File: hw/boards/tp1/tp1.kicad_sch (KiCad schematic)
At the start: 17 parts

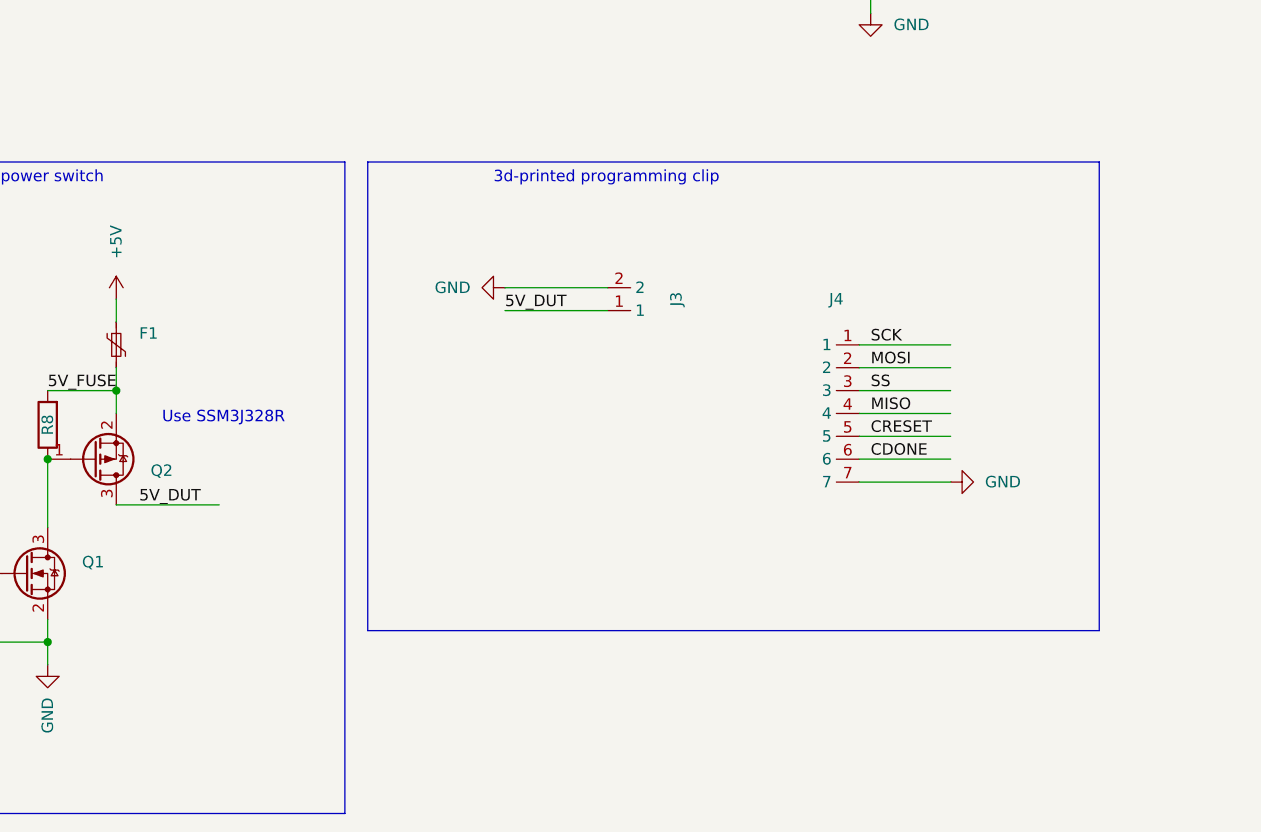
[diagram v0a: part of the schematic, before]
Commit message: TP-1 release: Add screws, feet to the BOM
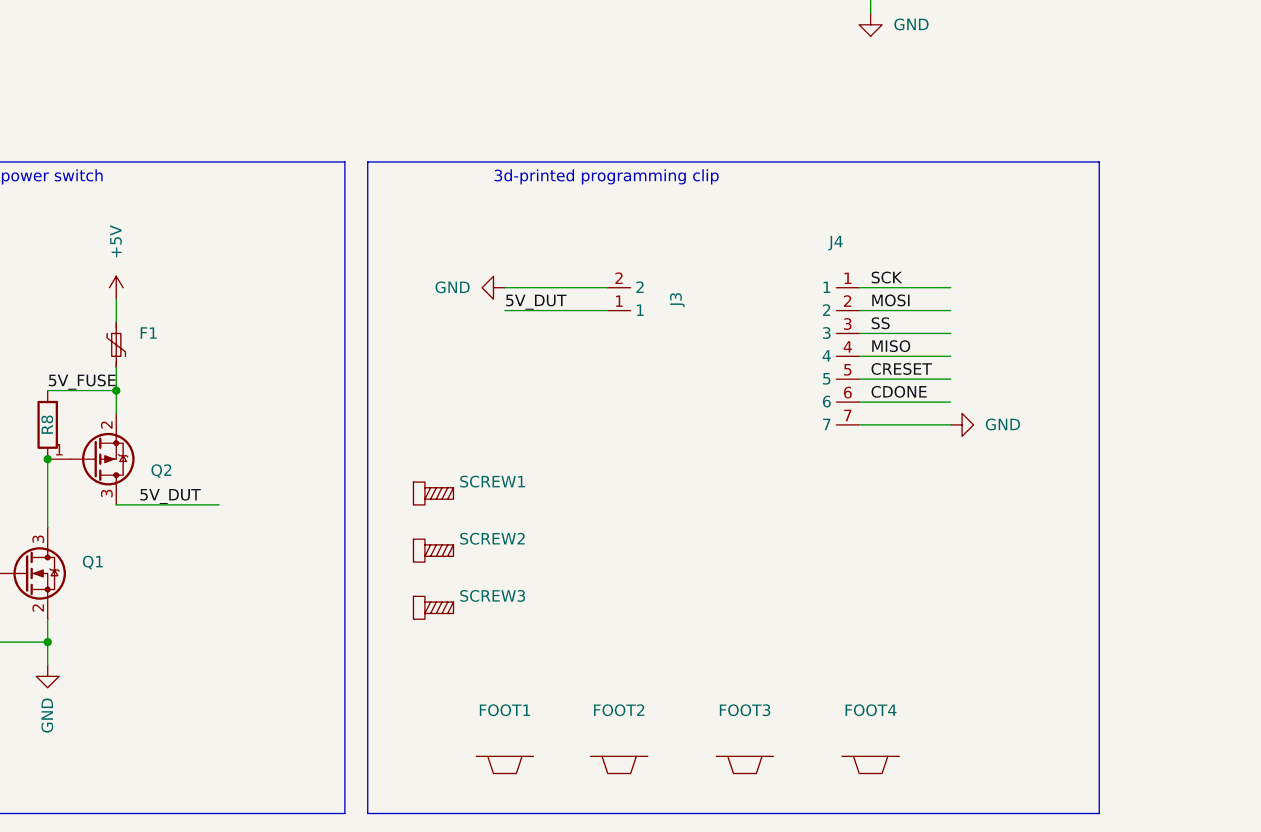
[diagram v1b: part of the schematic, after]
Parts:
- added FOOT1, FOOT2, FOOT3, FOOT4: (no value), symbol mta1:Foot
- added SCREW1, SCREW2, SCREW3: (no value), symbol mta1:Screw
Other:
- note removed: "Use SSM3J328R"
- moved on the sheet: J4

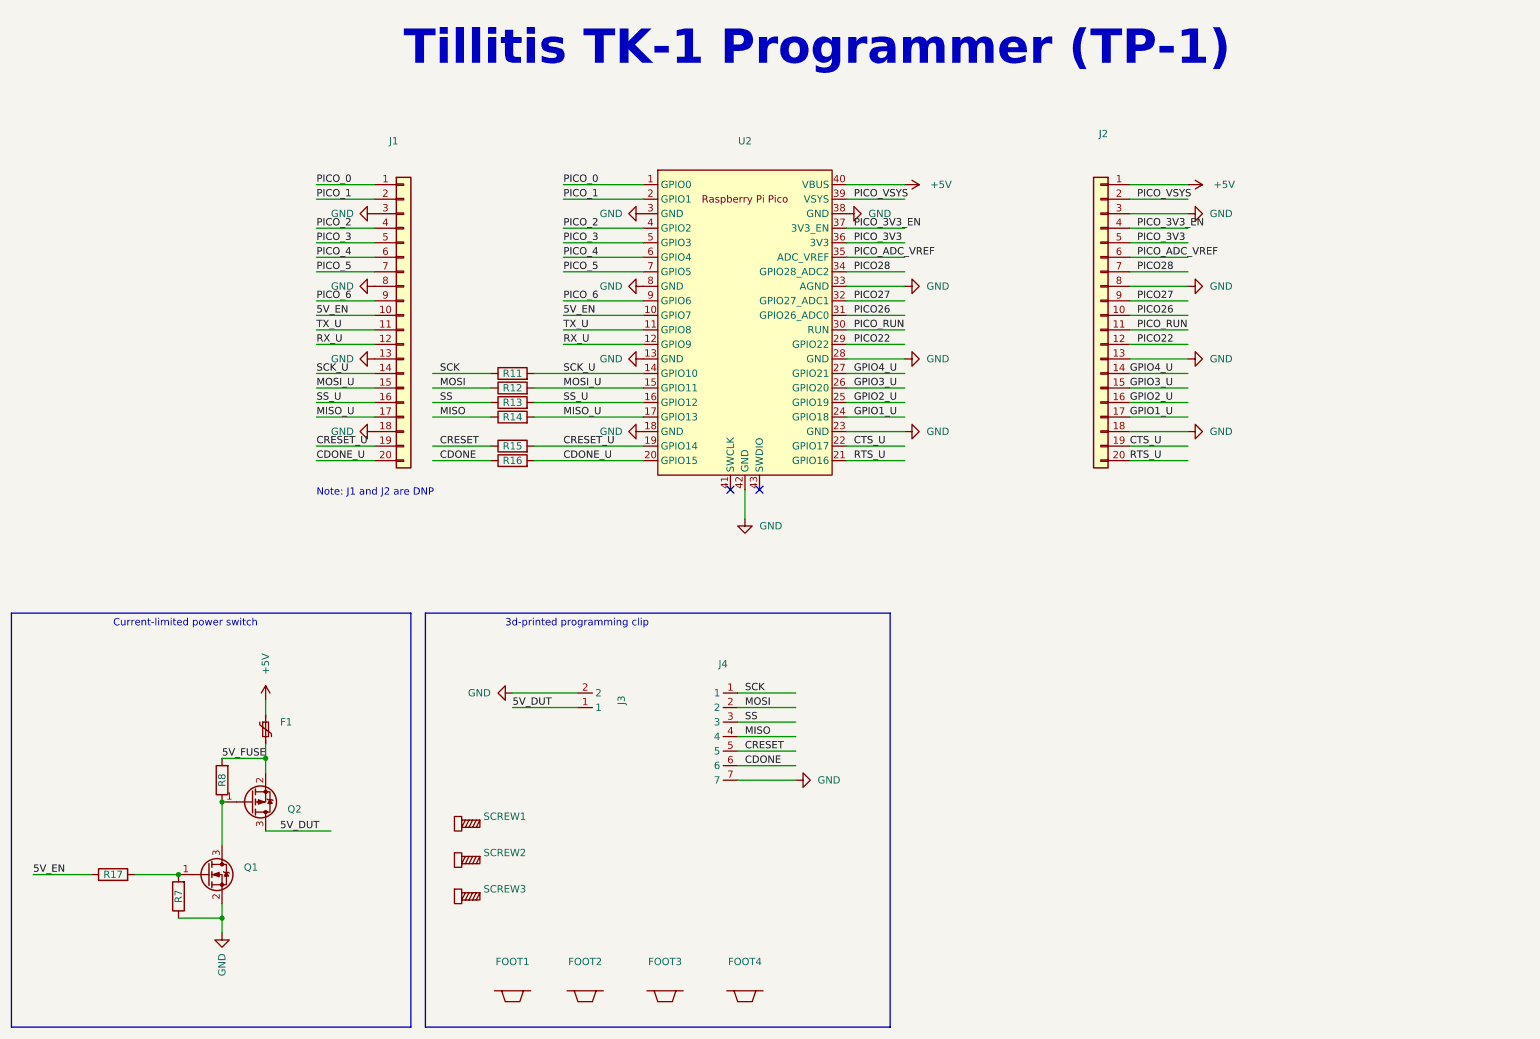
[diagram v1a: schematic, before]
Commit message: TP-1 RevA release updates:
* Add fiducials in 3 corners (1mm exposed copper ring w/2mm soldermask opening)
* Add solder paste openings to Raspberry Pi Pico pads
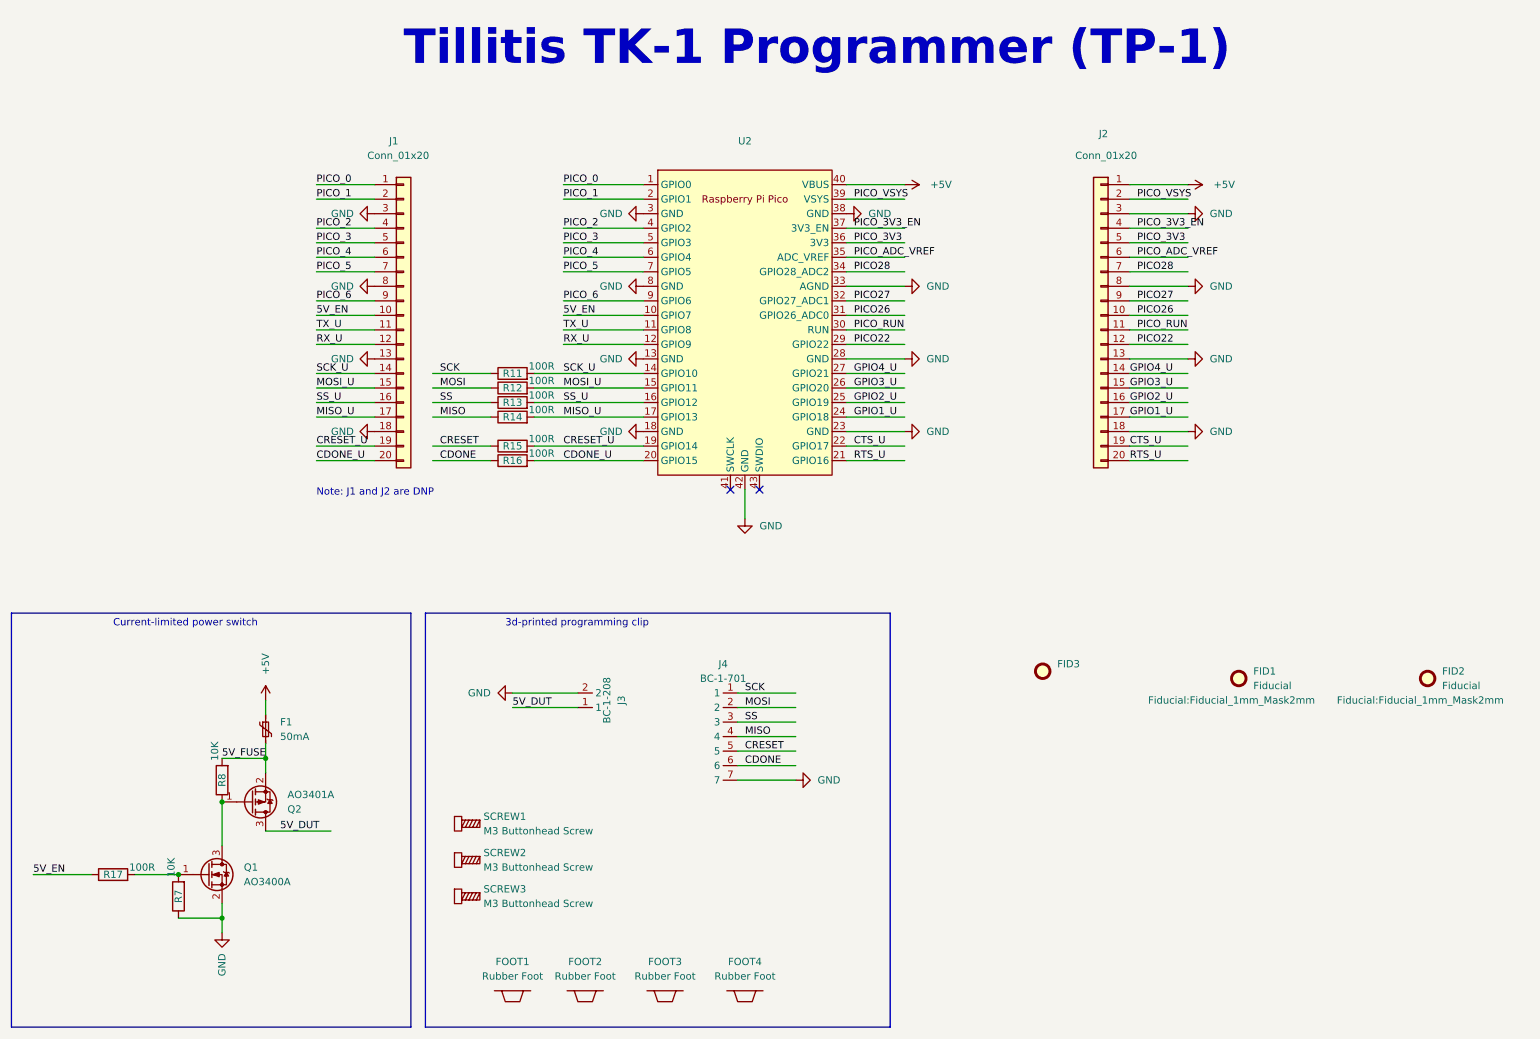
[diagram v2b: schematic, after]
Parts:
- added FID1, FID2: Fiducial, Fiducial:Fiducial_1mm_Mask2mm, symbol Mechanical:Fiducial
- added FID3: (no value), symbol Mechanical:Fiducial
- F1: value (none) -> 50mA; footprint (none) -> Fuse:Fuse_1206_3216Metric
- FOOT1, FOOT2, FOOT3, FOOT4: value (none) -> Rubber Foot
- J1, J2: value (none) -> Conn_01x20; footprint (none) -> Connector_PinHeader_2.54mm:PinHeader_1x20_P2.54mm_Vertical
- J3: value (none) -> BC-1-208; footprint (none) -> mta1:BC-1-208
- J4: value (none) -> BC-1-701; footprint (none) -> mta1:BC-1-701
- Q1: value (none) -> AO3400A; footprint (none) -> Package_TO_SOT_SMD:SOT-23
- Q2: value (none) -> AO3401A; footprint (none) -> Package_TO_SOT_SMD:SOT-23
- R11, R12, R13, R14, R15, R16, R17: value (none) -> 100R; footprint (none) -> mta1:ERJ2G(0402)_L
- R7, R8: value (none) -> 10K; footprint (none) -> mta1:ERJ2G(0402)_L
- SCREW1, SCREW2, SCREW3: value (none) -> M3 Buttonhead Screw

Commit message: TP-1: Update fuse type to match actual part
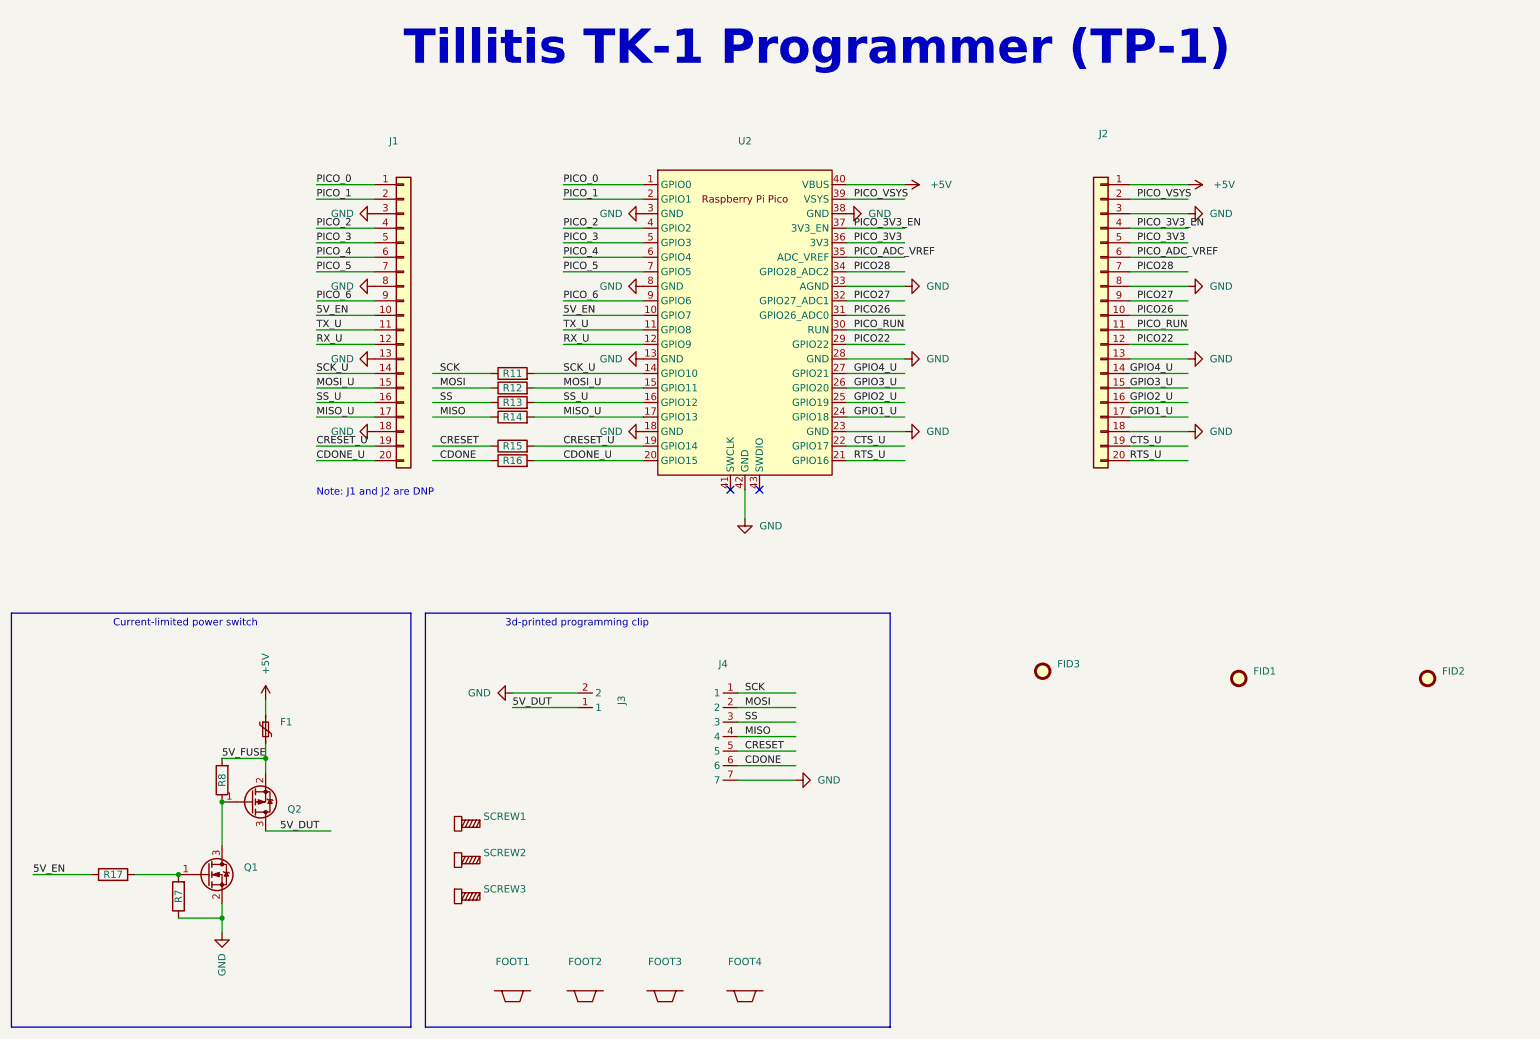
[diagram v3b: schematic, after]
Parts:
- F1: value 50mA -> (none); footprint Fuse:Fuse_1206_3216Metric -> (none); Manufacturer Bel Fuse -> Littelfuse; Manufacturer Part Number 0ZCJ0005FF2E -> 1206L005/60WR; Supplier Part Number 507-1793-2-ND -> F8129TR-ND
- FID1, FID2: value Fiducial -> (none); footprint Fiducial:Fiducial_1mm_Mask2mm -> (none)
- FOOT1, FOOT2, FOOT3, FOOT4: value Rubber Foot -> (none)
- J1, J2: value Conn_01x20 -> (none); footprint Connector_PinHeader_2.54mm:PinHeader_1x20_P2.54mm_Vertical -> (none)
- J3: value BC-1-208 -> (none); footprint mta1:BC-1-208 -> (none)
- J4: value BC-1-701 -> (none); footprint mta1:BC-1-701 -> (none)
- Q1: value AO3400A -> (none); footprint Package_TO_SOT_SMD:SOT-23 -> (none)
- Q2: value AO3401A -> (none); footprint Package_TO_SOT_SMD:SOT-23 -> (none)
- R11, R12, R13, R14, R15, R16, R17: value 100R -> (none); footprint mta1:ERJ2G(0402)_L -> (none)
- R7, R8: value 10K -> (none); footprint mta1:ERJ2G(0402)_L -> (none)
- SCREW1, SCREW2, SCREW3: value M3 Buttonhead Screw -> (none)
